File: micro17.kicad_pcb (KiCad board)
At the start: 2 copper layers, 20 x 30 mm, 72 parts, among them U1 STM32G473CCUx, U2 AMS1117-3.3, U3 AMS1117-5.0, U4 MCP6002, U5 MCP4451-503-ST, U6 MCP6002, U7 MCP6002, Y1 8 MHz

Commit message: PCB routed, gerbers and ibom included
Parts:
- removed C12: 22u/25V, Capacitor_SMD:C_0805_2012Metric
- removed J2, J3, J4: ~, TestPoint:TestPoint_Pad_D1.5mm
- removed U3: AMS1117-5.0, Package_TO_SOT_SMD:SOT-223-3_TabPin2
- added FB1: FerriteBead_Small, Capacitor_SMD:C_0603_1608Metric, F.Cu at (183.0, 63.8)
- added J5: AXK640347YG, Micro17-ICOM_Board:AXK640347YG, B.Cu at (190.0, 76.0)
- added SYM1: SYM_ESD_Small, Symbol:ESD-Logo_6.6x6mm_SilkScreen, F.Cu at (185.2, 53.2)
- added SYM2: Logo_Open_Hardware_Small, Symbol:OSHW-Logo_5.7x6mm_SilkScreen, B.Cu at (194.0, 60.8)
- added TP2: TP_TX, TestPoint:TestPoint_Pad_D1.0mm, F.Cu at (190.8, 78.8)
- C1, C11, C13, C14, C15, C16, C17, C18, C19, C2, C20, C22, C23, C24, C25, C3, C30, C31, C33, C35, C4, C5, C6, C7, C8, C9: footprint Capacitor_SMD:C_0201_0603Metric -> Capacitor_SMD:C_0402_1005Metric
- C21, C29, C32: footprint Capacitor_SMD:C_0805_2012Metric -> Capacitor_SMD:C_0402_1005Metric
- J1: value ~ -> Conn_01x04; footprint TestPoint:TestPoint_Pad_D1.5mm -> Connector_Harwin:Harwin_M20-89004xx_1x04_P2.54mm_Horizontal
- R1, R10, R11, R12, R13, R14, R15, R16, R17, R2, R20, R21, R22, R23, R3, R4, R5, R6, R7, R8, R9: footprint Resistor_SMD:R_0201_0603Metric -> Resistor_SMD:R_0402_1005Metric
- R18: value 0 -> 3k3; footprint Resistor_SMD:R_0201_0603Metric -> Resistor_SMD:R_0402_1005Metric
- R19: value DNP -> 3k3; footprint Resistor_SMD:R_0201_0603Metric -> Resistor_SMD:R_0402_1005Metric
- R24: footprint Resistor_SMD:R_0201_0603Metric -> Resistor_SMD:R_0603_1608Metric
- U2: value AMS1117-3.3 -> XC6220B331MR; footprint Package_TO_SOT_SMD:SOT-223-3_TabPin2 -> Package_TO_SOT_SMD:SOT-23-5; moved to F.Cu
- moved C15 85.5 mm to (198.2, 71.9), turned to 90 degrees
- moved C34 84.8 mm to (191.2, 75.4), turned to -90 degrees
- moved C20 83.1 mm to (199.2, 70.0), turned to 90 degrees
- moved C28 82.8 mm to (194.9, 71.2)
- moved C33 82.2 mm to (195.4, 76.7)
- moved R7 82.1 mm to (199.3, 73.9), turned to 90 degrees
- moved C3 81.8 mm to (198.8, 55.8), turned to 90 degrees
- moved C18 81.8 mm to (196.7, 69.5), turned to 180 degrees
- moved C29 81.8 mm to (197.4, 77.8)
- moved C30 81.7 mm to (198.8, 66.8), turned to 90 degrees
- moved C5 81.0 mm to (198.8, 64.8), turned to -90 degrees
- moved R22 80.4 mm to (197.4, 76.7), turned to 180 degrees
- moved J1 79.8 mm to (194.3, 46.5), turned to 90 degrees
- moved R9 79.8 mm to (199.2, 71.9), turned to 90 degrees
- moved C27 79.7 mm to (188.6, 75.4), turned to -90 degrees
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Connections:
- C10 pad 1: VDC -> +5V
- C16 pad 1: /Filtering/BASEBAND_IN_FILT -> BASEBAND_IN_FILT
- C22 pad 2: /Filtering/AUDIO_OUT_FILT -> AUDIO_OUT_FILT
- C23 pad 2: /Filtering/AUDIO_IN_FILT -> AUDIO_IN_FILT
- C27 pad 2: Net-(C27-Pad2) -> BASEBAND_IN
- C34 pad 2: /Filtering/BASEBAND_OUT_FILT -> BASEBAND_OUT_FILT
- R18 pad 1: /Filtering/BASEBAND_IN -> +3V3
- R18 pad 2: Net-(C27-Pad2) -> I2C_SCL
- R19 pad 1: Net-(C27-Pad2) -> +3V3
- R19 pad 2: GND -> I2C_SDA
- R20 pad 1: VDD -> +5V
- R4 pad 1: /MCU/PTT_IN -> PTT_IN
- R6 pad 1: /Filtering/AUDIO_OUT -> AUDIO_OUT
- R7 pad 1: /Filtering/AUDIO_IN -> AUDIO_IN
- TP1 pad 1: Net-(C27-Pad2) -> BASEBAND_IN
- U1 pad 10: /MCU/AUDIO_IN_FILT -> AUDIO_IN_FILT
- U1 pad 12: /MCU/BASEBAND_OUT -> BASEBAND_OUT
- U1 pad 13: /MCU/AUDIO_OUT -> AUDIO_OUT
- U1 pad 14: /MCU/PTT_OUT -> PTT_OUT
- U1 pad 18: /MCU/AUDIO_OUT_MUTE -> AUDIO_OUT_MUTE
- U1 pad 31: /MCU/MCU_TX -> MCU_TX
- U1 pad 32: /MCU/MCU_RX -> MCU_RX
- U1 pad 38: unconnected-(U1-PA15-Pad38) -> I2C_SCL
- U1 pad 47: unconnected-(U1-PB9-Pad47) -> I2C_SDA
- U1 pad 9: /MCU/BASEBAND_IN_FILT -> BASEBAND_IN_FILT
- U2 pad 1: GND -> +5V
- U2 pad 2: +3V3 -> GND
- U2 pad 3: VDC -> +5V
- U4 pad 6: /Filtering/BASEBAND_IN_FILT -> BASEBAND_IN_FILT
- U4 pad 7: /Filtering/BASEBAND_IN_FILT -> BASEBAND_IN_FILT
- U5 pad 20: /Filtering/BASEBAND_OUT -> BASEBAND_OUT
- U5 pad 5: /Filtering/I2C_SCL -> I2C_SCL
- U5 pad 6: /Filtering/I2C_SDA -> I2C_SDA
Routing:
- net +3V3: track 0.00 -> 62.7 mm, vias 0 -> 7
- net +5V: track 0.00 -> 44.6 mm, vias 0 -> 5
- net PTT_IN: track 0.00 -> 38.5 mm, vias 0 -> 2
- net Net-(U5B-P1A): track 0.00 -> 28.1 mm, vias 0 -> 2
- net GND: track 0.00 -> 25.6 mm, vias 0 -> 53
- net MCU_TX: track 0.00 -> 24.0 mm, vias 0 -> 3
- net I2C_SCL: track 0.00 -> 23.6 mm, vias 0 -> 2
- net I2C_SDA: track 0.00 -> 22.7 mm, vias 0 -> 2
- net Net-(U5A-P0A): track 0.00 -> 20.5 mm, vias 0 -> 3
- net MCU_RX: track 0.00 -> 19.6 mm, vias 0 -> 1
- net Net-(U5C-P2W): track 0.00 -> 16.9 mm, vias 0 -> 2
- net AUDIO_OUT_MUTE: track 0.00 -> 16.9 mm, vias 0 -> 1
- net BASEBAND_OUT: track 0.00 -> 16.7 mm, vias 0 -> 2
- net PTT_OUT: track 0.00 -> 12.5 mm, vias 0 -> 2
- net AUDIO_IN: track 0.00 -> 11.6 mm, vias 0 -> 1
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- added copper zone on B.Cu, net GND
- added copper zone on F.Cu, net GND
- added copper zone on In1.Cu, net GND
- added copper zone on In2.Cu, net GND
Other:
- copper layers 2 -> 4
- board text added: "ON6RF & TA1MD UT-M17_v1.0 2024"

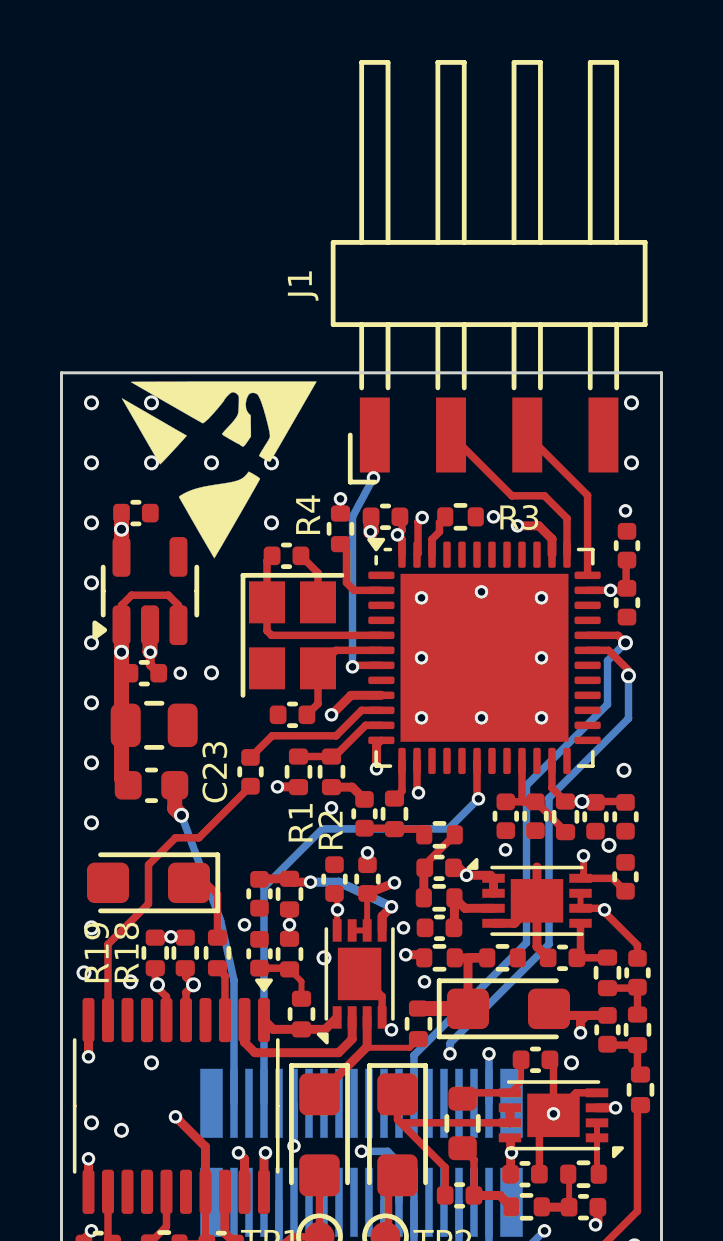
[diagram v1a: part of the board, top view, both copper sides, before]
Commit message: Updates
GP relay added,
3v3 added to programming conn.
diode(dnp) added for motorola type internal bus.
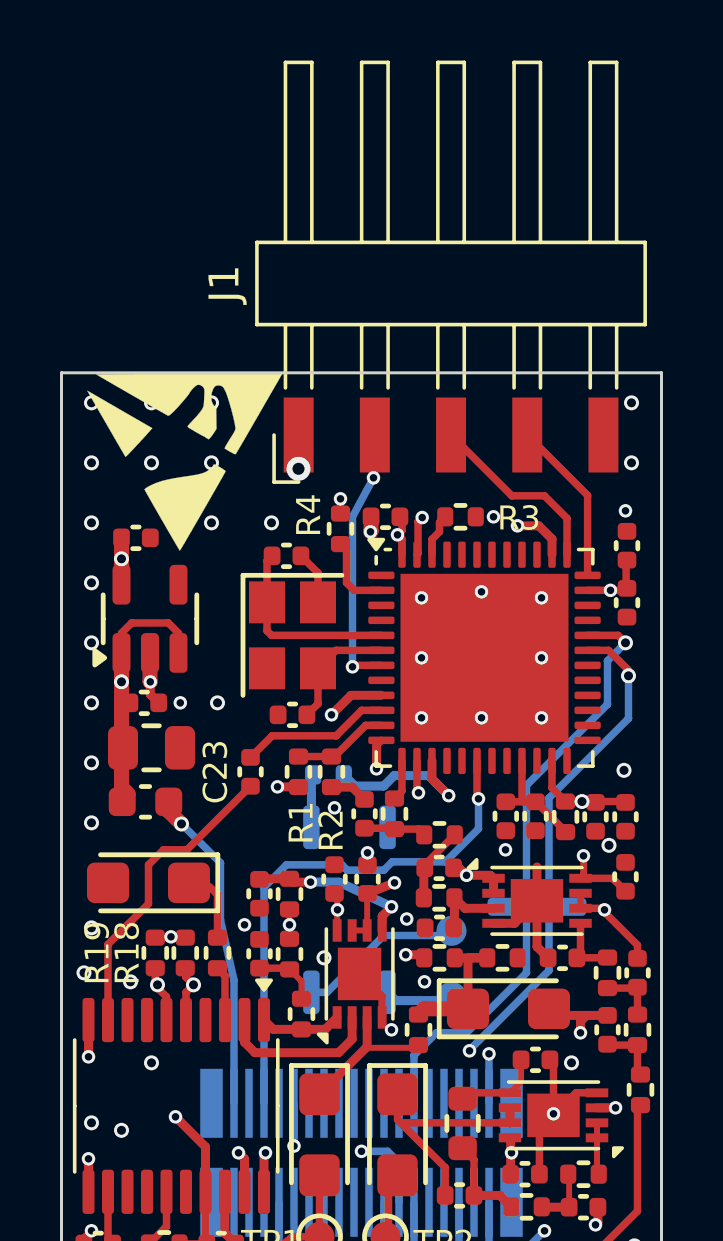
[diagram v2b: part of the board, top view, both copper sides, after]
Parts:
- added D1: 1N4148WS, Diode_SMD:D_SOD-323, B.Cu at (195.8, 67.8)
- added R25: 3k3, Resistor_SMD:R_0402_1005Metric, B.Cu at (188.9, 63.4)
- added TP3: GP, TestPoint:TestPoint_Pad_D1.0mm, B.Cu at (193.0, 68.6)
- added TP4: GP, TestPoint:TestPoint_Pad_D1.0mm, B.Cu at (193.0, 70.8)
- added U3: CPC1117N, Package_SO:SOP-4_3.8x4.1mm_P2.54mm, B.Cu at (189.6, 67.9)
- J1: value Conn_01x04 -> Conn_01x05; footprint Connector_Harwin:Harwin_M20-89004xx_1x04_P2.54mm_Horizontal -> Connector_Harwin:Harwin_M20-89005xx_1x05_P2.54mm_Horizontal
- moved J1 1.27 mm to (193.0, 46.5)
- moved SYM1 1.18 mm to (184.1, 53.0)
- moved C13 0.99 mm to (182.8, 61.0)
- moved U2 0.93 mm to (182.9, 58.2)
- moved C11 0.82 mm to (182.5, 55.5)
- moved C10 0.76 mm to (183.0, 62.5)
- moved FB1 0.59 mm to (182.8, 64.3)
- moved R17 0.20 mm to (191.9, 71.9)
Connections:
- net Net-(J5-Pin_38) renamed +5VD
- J1 pad 1: /MCU/~{RST} -> +3V3
- J1 pad 2: /MCU/SWCLK -> /MCU/~{RST}
- J1 pad 3: /MCU/SWDIO -> /MCU/SWCLK
- J1 pad 4: GND -> /MCU/SWDIO
- U1 pad 15: unconnected-(U1-PA7-Pad15) -> BASEBAND_BYPASS
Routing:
- net Net-(TP3-Pad1): track 0.00 -> 5.52 mm
- net BASEBAND_BYPASS: track 0.00 -> 5.46 mm, vias 0 -> 1
- net +3V3: track 62.7 -> 66.6 mm, vias 7 -> 8
- net Net-(TP4-Pad1): track 0.00 -> 2.30 mm
- net Net-(R25-Pad2): track 0.00 -> 1.77 mm
- net +5V: track 44.6 -> 43.0 mm
- net AUDIO_OUT_MUTE: track 16.9 -> 17.6 mm
- net MCU_RX: track 19.6 -> 20.2 mm
- net GND: track 25.6 -> 25.7 mm, vias 53 -> 51

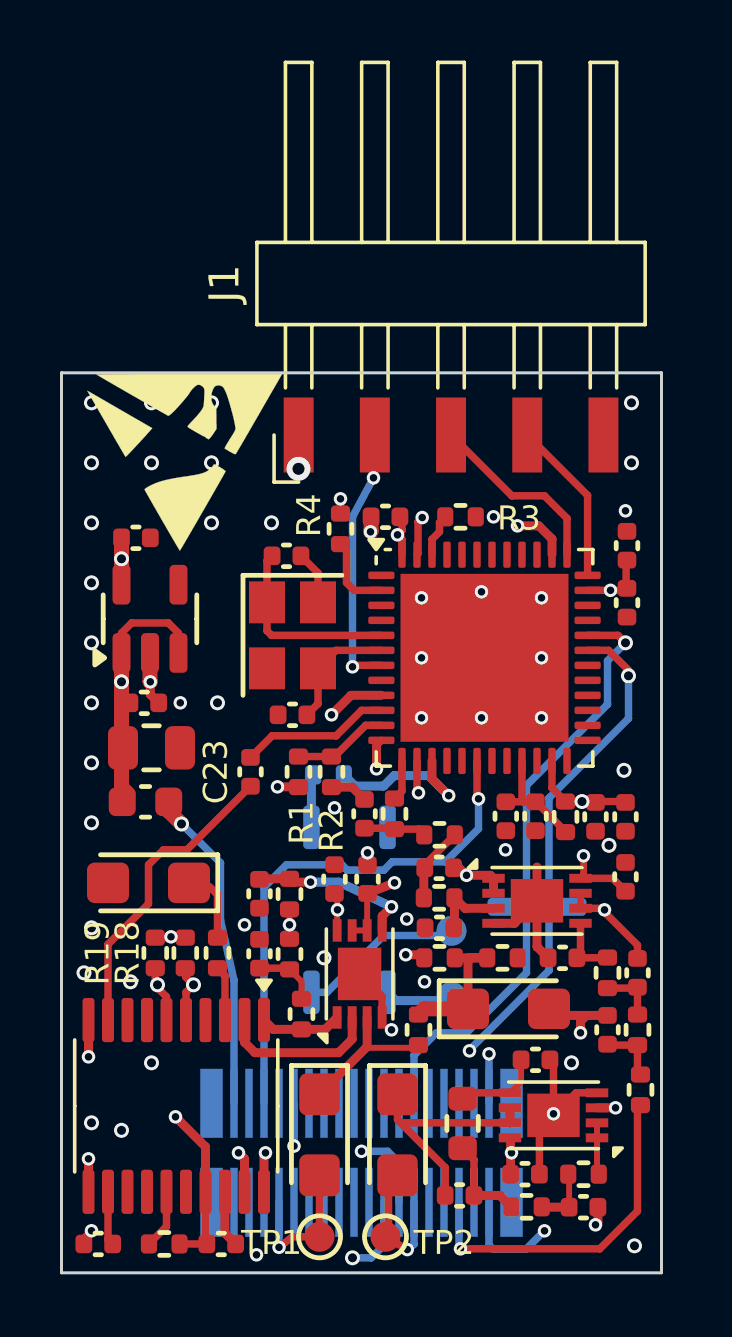
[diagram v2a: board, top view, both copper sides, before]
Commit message: J2 Corrected, More TP added.
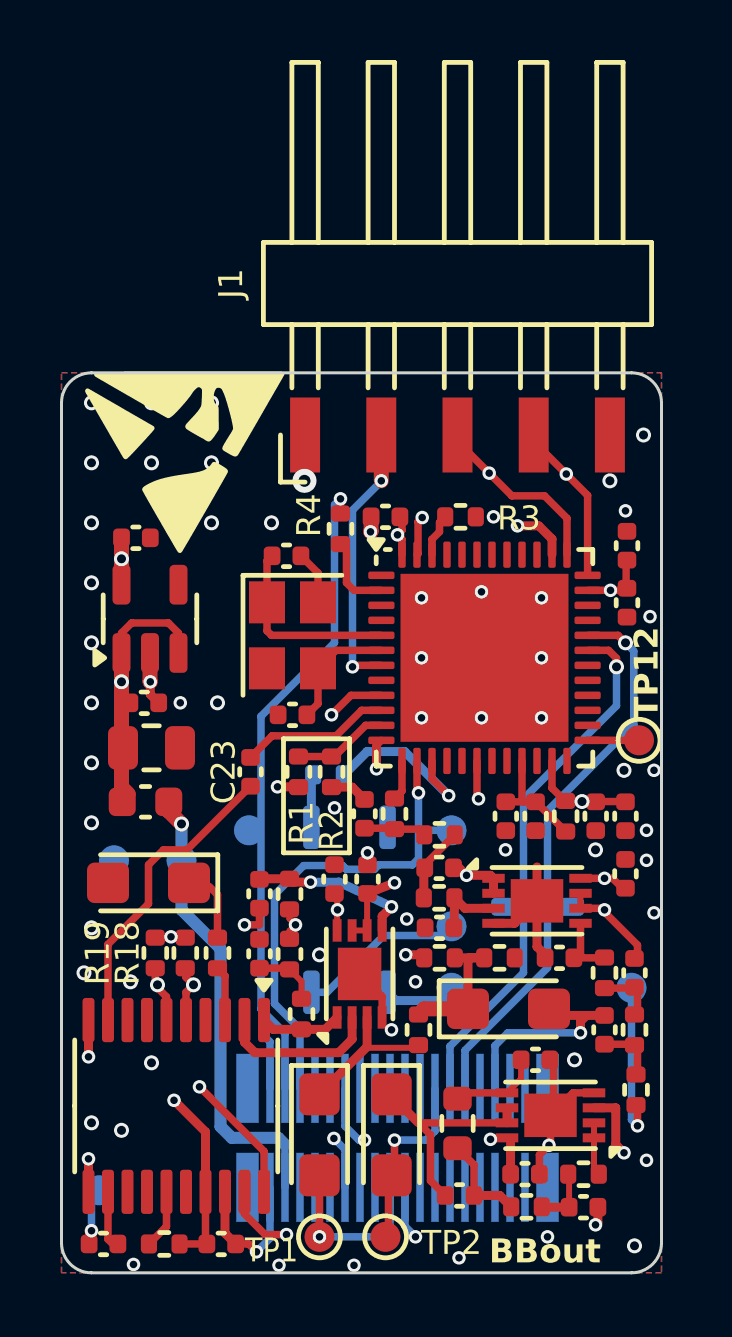
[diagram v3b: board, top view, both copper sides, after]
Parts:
- removed J5: AXK640347YG, Micro17-ICOM_Board:AXK640347YG
- added J2: AXK640347YG, micro17:AXK640347YG, B.Cu at (191.2, 75.5)
- added TP10: GP, TestPoint:TestPoint_Pad_D1.0mm, B.Cu at (181.8, 66.2)
- added TP12: GP, TestPoint:TestPoint_Pad_D1.0mm, F.Cu at (199.2, 62.2)
- added TP5: GP, TestPoint:TestPoint_Pad_D1.0mm, B.Cu at (184.0, 66.2)
- added TP6: GP, TestPoint:TestPoint_Pad_D1.0mm, B.Cu at (193.0, 65.2)
- added TP7: GP, TestPoint:TestPoint_Pad_D1.0mm, B.Cu at (186.2, 65.2)
- added TP8: GP, TestPoint:TestPoint_Pad_D1.0mm, B.Cu at (199.0, 70.5)
- added TP9: GP, TestPoint:TestPoint_Pad_D1.0mm, B.Cu at (181.2, 77.2)
- moved SYM2 2.50 mm to (194.0, 58.2)
- moved TP4 0.30 mm to (193.0, 70.5)
- moved J1 0.21 mm to (193.2, 46.5)
- moved C34 0.20 mm to (191.0, 75.4)
- moved C22 0.18 mm to (181.4, 79.0)
- moved R24 0.17 mm to (193.2, 75.0)
- moved R7 0.15 mm to (199.2, 73.9)
- moved TP3 0.15 mm to (193.0, 68.5)
- moved C15 0.10 mm to (198.1, 71.9)
- moved C18 0.10 mm to (196.6, 69.5)
- moved C20 0.10 mm to (199.1, 70.0)
- moved C30 0.10 mm to (198.8, 66.7)
- moved R11 0.10 mm to (198.1, 70.0)
- moved R21 0.10 mm to (194.6, 69.5)
- moved R9 0.10 mm to (199.1, 71.9)
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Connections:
- U1 pad 25: unconnected-(U1-PB12-Pad25) -> Net-(U1-PB12)
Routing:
- net PTT_IN: track 38.5 -> 21.6 mm, vias 2 -> 1
- net GND: track 25.7 -> 33.5 mm, vias 51 -> 61
- net MCU_TX: track 24.2 -> 18.3 mm, vias 3 -> 1
- net AUDIO_IN: track 11.6 -> 17.4 mm, vias 1 -> 2
- net +5VD: track 10.8 -> 15.4 mm
- net AUDIO_OUT_FILT: track 10.3 -> 14.7 mm
- net PTT_OUT: track 12.5 -> 16.6 mm, vias 2 -> 1
- net Net-(U1-PB12): track 0.00 -> 1.71 mm
- net BASEBAND_OUT_FILT: track 4.62 -> 6.21 mm
- net +5V: track 43.0 -> 41.4 mm
- net BASEBAND_OUT: track 16.8 -> 18.2 mm
- net AUDIO_OUT_MUTE: track 17.6 -> 16.2 mm, vias 1 -> 2
- net BASEBAND_IN: track 5.02 -> 5.92 mm
- net MCU_RX: track 20.2 -> 19.4 mm
- net Net-(U7B--): track 8.93 -> 8.23 mm
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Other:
- outline, holes or cut-outs redrawn
- board text added: "5V"
- board text added: "Ain"
- board text added: "Aout"
- board text added: "BBout"
- board text added: "Gnd"
- board text added: "PttIn"
- board text added: "PttOut"

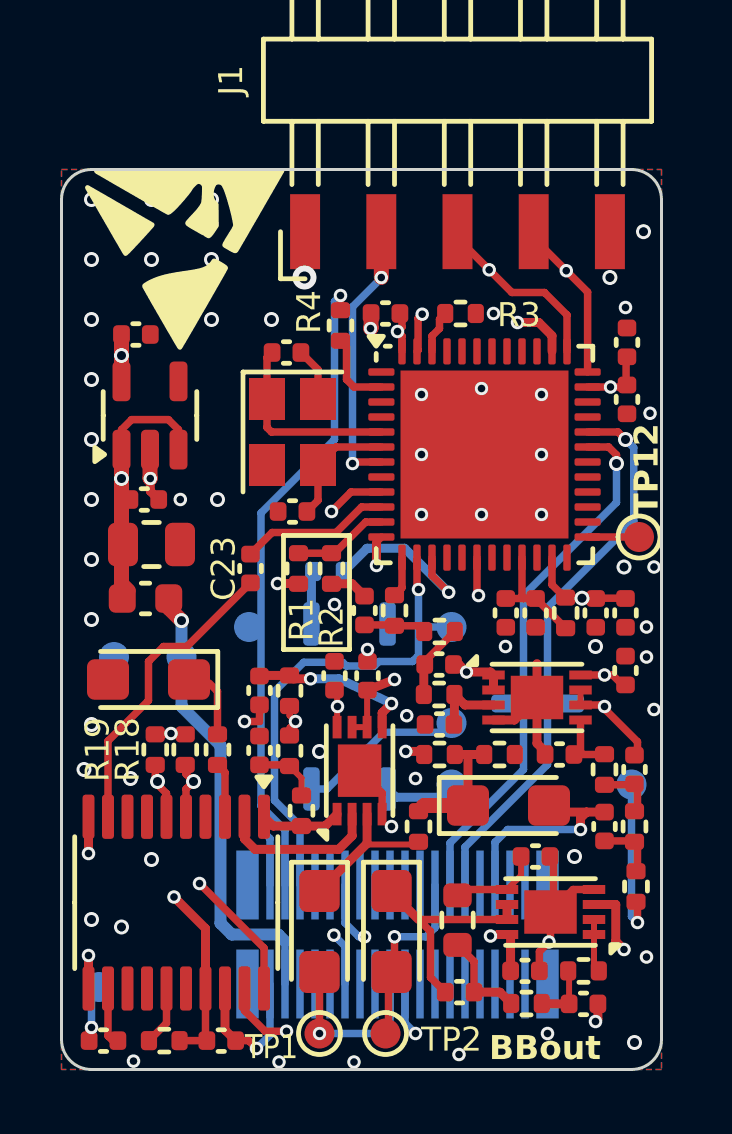
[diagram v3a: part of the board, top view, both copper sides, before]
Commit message: PA2 Bias add, USB conn add.
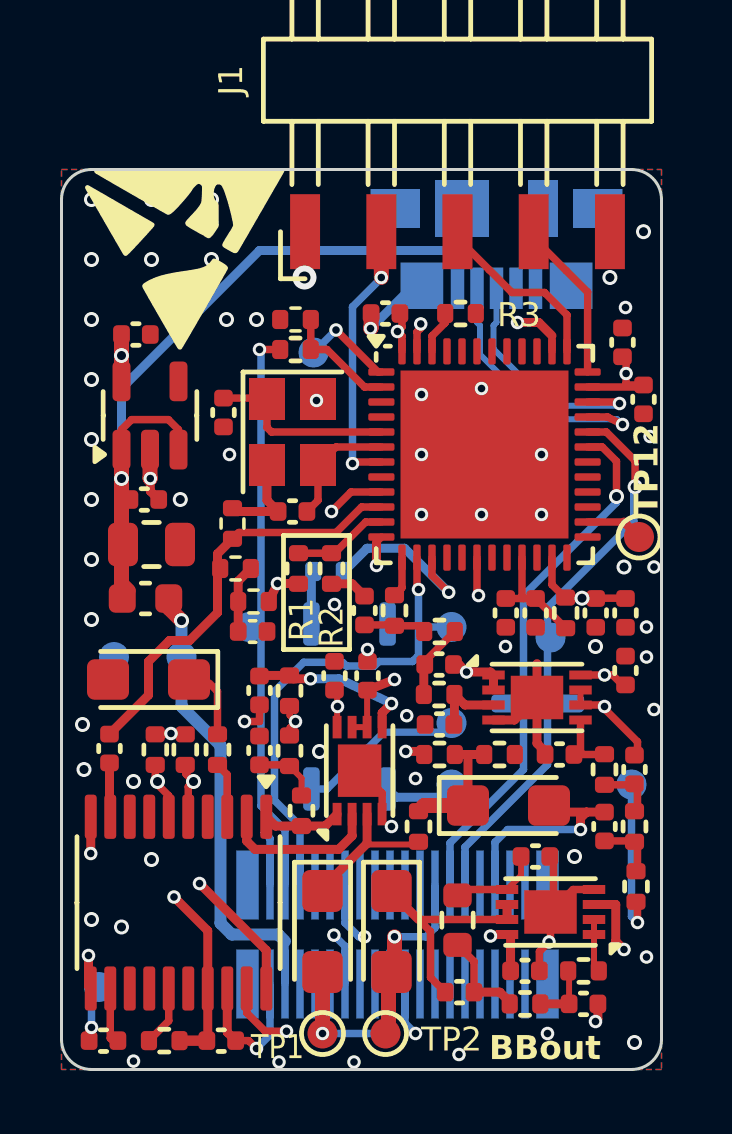
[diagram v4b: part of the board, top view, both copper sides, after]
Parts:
- added C12: 220n, Capacitor_SMD:C_0402_1005Metric, F.Cu at (186.4, 65.4)
- added J4: USB_B_Micro, Connector_USB:USB_Micro-B_Molex_47346-0001, B.Cu at (194.5, 52.5)
- added R26: 10k, Resistor_SMD:R_0402_1005Metric, F.Cu at (185.8, 63.3)
- added R27: 22k, Resistor_SMD:R_0402_1005Metric, F.Cu at (185.7, 61.8)
- added R28: 12k, Resistor_SMD:R_0402_1005Metric, F.Cu at (186.4, 64.4)
- added R29: 12k, Resistor_SMD:R_0402_1005Metric, F.Cu at (187.8, 55.0)
- added TP11: GP, TestPoint:TestPoint_Pad_D1.0mm, B.Cu at (188.4, 56.1)
- added TP13: GP, TestPoint:TestPoint_Pad_D1.0mm, B.Cu at (196.3, 65.6)
- moved C23 7.62 mm to (181.6, 69.3)
- moved C1 2.90 mm to (185.4, 58.1), turned to -90 degrees
- moved SYM2 1.81 mm to (195.8, 58.4)
- moved R4 1.70 mm to (187.8, 56.0), turned to 0 degrees
- moved C6 0.55 mm to (199.4, 57.7)
- moved C3 0.15 mm to (198.7, 55.8)
- moved C27 0.10 mm to (188.7, 75.4)
- moved TP1 0.10 mm to (188.7, 78.8)
- moved U5 0.08 mm to (183.9, 74.4)
- moved R23 0.05 mm to (195.4, 77.8)
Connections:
- net /MCU/VERSION_SET renamed VERSION_SET
- TP12 pad 1: Net-(U1-PB12) -> Net-(U1-PB13)
- U1 pad 1: unconnected-(U1-VBAT-Pad1) -> Net-(U1-VBAT)
- U1 pad 25: Net-(U1-PB12) -> unconnected-(U1-PB12-Pad25)
- U1 pad 26: unconnected-(U1-PB13-Pad26) -> Net-(U1-PB13)
- U1 pad 33: unconnected-(U1-PA11-Pad33) -> USB_DN
- U1 pad 34: unconnected-(U1-PA12-Pad34) -> USB_DP
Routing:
- net +5V: track 41.4 -> 58.6 mm
- net USB_DN: track 0.00 -> 9.09 mm, vias 0 -> 1
- net AUDIO_IN_FILT: track 5.01 -> 14.0 mm
- net Net-(U5B-P1W): track 10.2 -> 1.81 mm
- net USB_DP: track 0.00 -> 8.06 mm, vias 0 -> 1
- net GND: track 33.5 -> 37.2 mm, vias 61 -> 60
- net Net-(U1-VBAT): track 0.00 -> 3.15 mm, vias 0 -> 1
- net +3V3: track 66.3 -> 69.2 mm
- net PTT_IN: track 21.6 -> 18.9 mm
- net Net-(C12-Pad1): track 0.00 -> 2.27 mm
- net Net-(U1-PB13): track 0.00 -> 1.92 mm
- net Net-(U1-PB12): track 1.71 -> 0.00 mm
- net Net-(U1-PC13): track 2.64 -> 3.87 mm
- net I2C_SDA: track 22.7 -> 22.1 mm
- net /MCU/SWDIO: vias 1 -> 0
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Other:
- board text added: "SBUS"
- board text added: "SP5WWP ON6RF TA1MD UT-M17_v1.0 2024"
- board text removed: "ON6RF & TA1MD UT-M17_v1.0 2024"
